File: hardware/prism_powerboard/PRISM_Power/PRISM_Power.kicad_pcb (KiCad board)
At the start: 2 copper layers, 48 parts, among them IC2 LP87564WRNFTQ1, J1 UJ32-21-C-H-G-HMT-LT-P24-TR, Q1 AO3400A, Q2 AO3400A, U1 STM32G031F6Px, U2 BQ25895RTW, U3 BQ297xy, U4 MAX17048G+T10

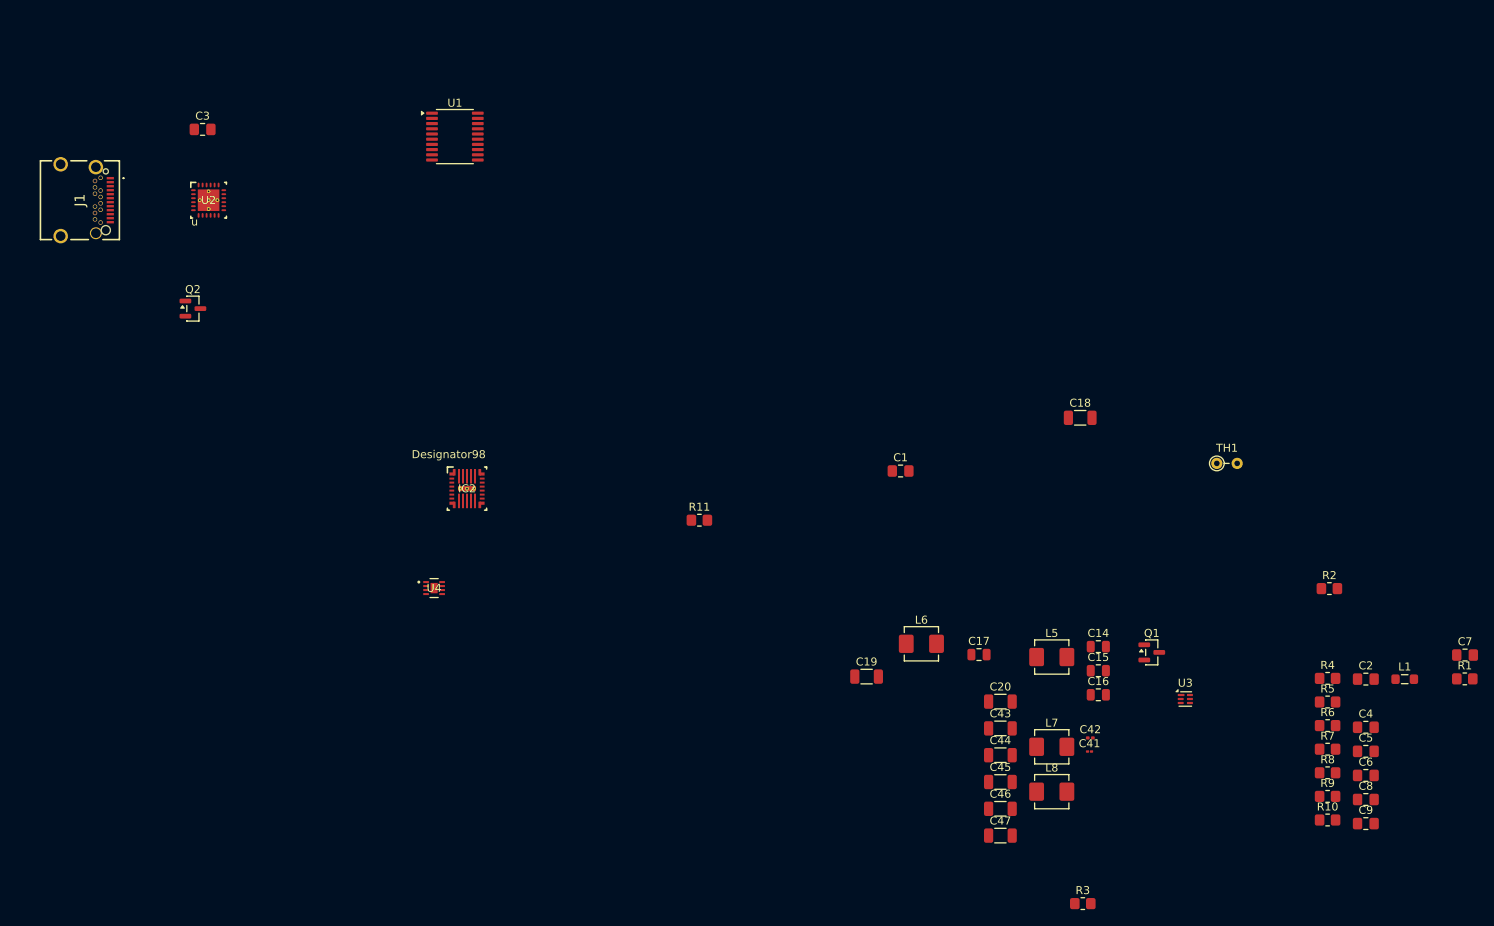
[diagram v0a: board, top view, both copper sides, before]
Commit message: PCB Routing
More PCB Routing and organizing components. Also fixed PMIC wrong Voltage labels/nets.
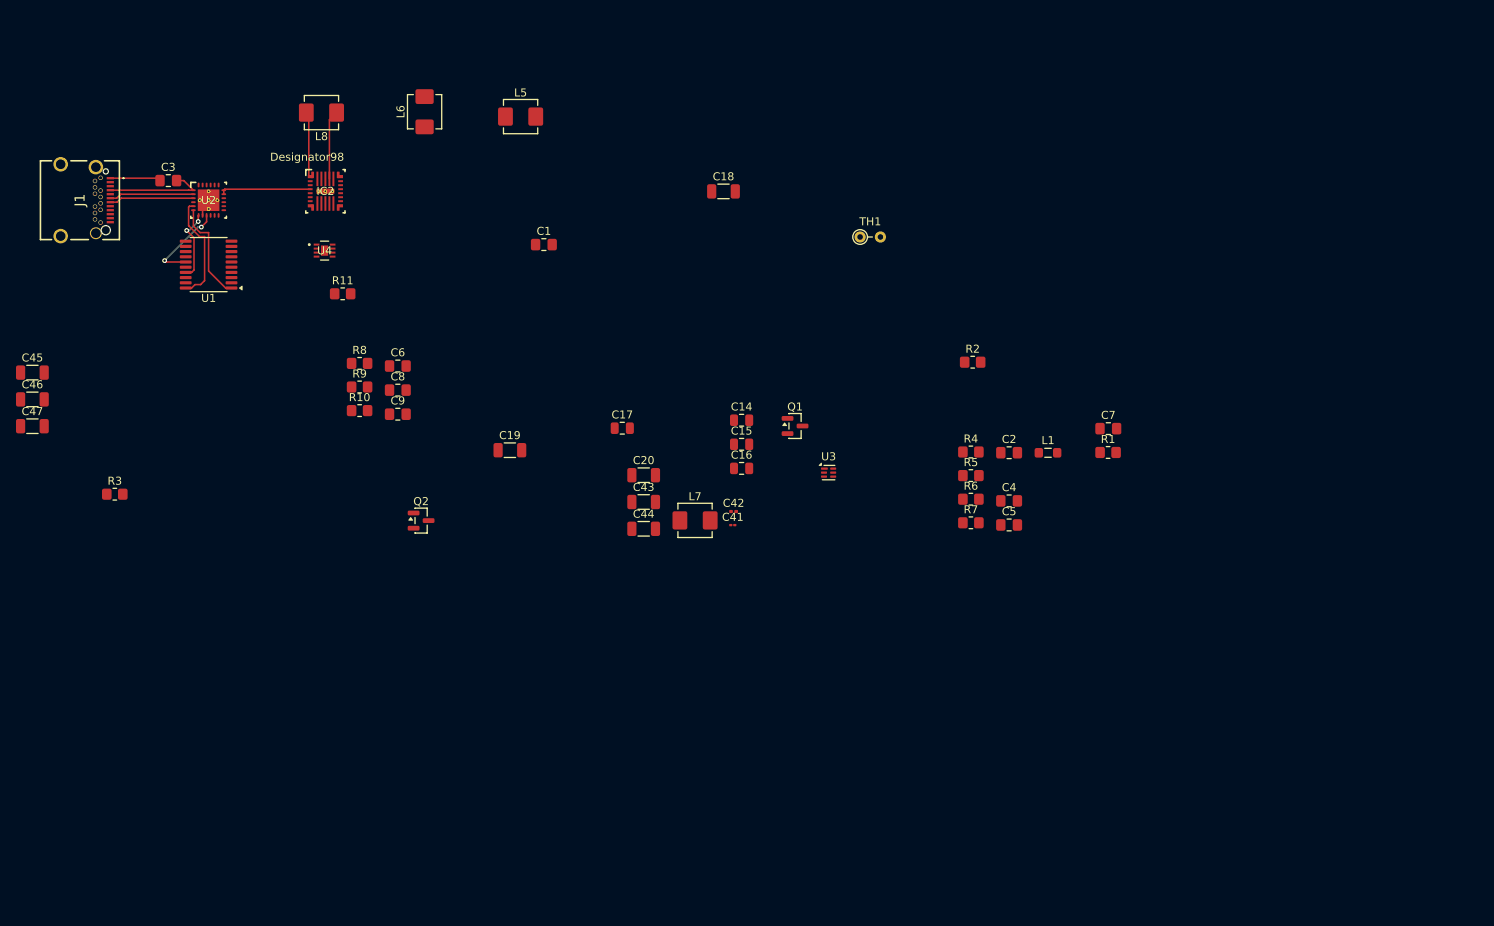
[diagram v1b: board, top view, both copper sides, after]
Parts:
- moved C45 131.4 mm to (76.5, 86.5)
- moved C46 131.4 mm to (76.5, 89.8)
- moved C47 131.4 mm to (76.5, 93.2)
- moved C6 131.4 mm to (122.2, 85.7)
- moved C8 131.4 mm to (122.2, 88.7)
- moved C9 131.4 mm to (122.2, 91.7)
- moved R10 131.4 mm to (117.4, 91.2)
- moved R3 131.4 mm to (86.8, 101.7)
- moved R8 131.4 mm to (117.4, 85.3)
- moved R9 131.4 mm to (117.4, 88.3)
- moved L8 124.7 mm to (112.6, 54.0), turned to 180 degrees
- moved L5 94.7 mm to (137.5, 54.5)
- moved L6 91.0 mm to (125.5, 53.9), turned to 90 degrees
- moved C16 52.8 mm to (165.1, 98.5)
- moved C4 52.8 mm to (198.6, 102.5)
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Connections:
- C18 pad 1: FB_B1 -> FB_B0
- C20 pad 1: FB_B1 -> FB_B0
- C44 pad 1: FB_B1 -> FB_B2
- C45 pad 1: FB_B1 -> FB_B2
- C46 pad 1: FB_B1 -> FB_B3
- C47 pad 1: FB_B1 -> FB_B3
- IC2 pad 1: FB_B1 -> FB_B2
- IC2 pad 21: FB_B1 -> FB_B3
- IC2 pad 5: SCL -> I2C_SCL_1V8
- IC2 pad 6: SDA -> I2C_SDA_1V8
- IC2 pad 8: FB_B1 -> FB_B0
- L5 pad 2: FB_B1 -> FB_B0
- L7 pad 2: FB_B1 -> FB_B2
- L8 pad 2: FB_B1 -> FB_B3
- R1 pad 2: FB_B1 -> +1V8
- R2 pad 1: FB_B1 -> +1V8
- R5 pad 2: FB_B1 -> +1V8
- R6 pad 2: FB_B1 -> +1V8
- U1 pad 4: FB_B1 -> +1V8_LDO
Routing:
- net GND: track 0.00 -> 19.4 mm
- net I2C_SCL_1V8: track 0.00 -> 13.8 mm
- net USB_VCC: track 0.00 -> 13.0 mm
- net I2C_SDA_1V8: track 0.00 -> 12.8 mm
- net CE_CHRG: track 0.00 -> 10.8 mm, vias 0 -> 2
- net USB_D_Plus: track 0.00 -> 10.6 mm
- net USB_D_Minus: track 0.00 -> 10.6 mm
- net INT_CHRG: track 0.00 -> 9.17 mm, vias 0 -> 2
- net SW_B3: track 0.00 -> 8.66 mm
- net FB_B1: track 0.00 -> 8.13 mm

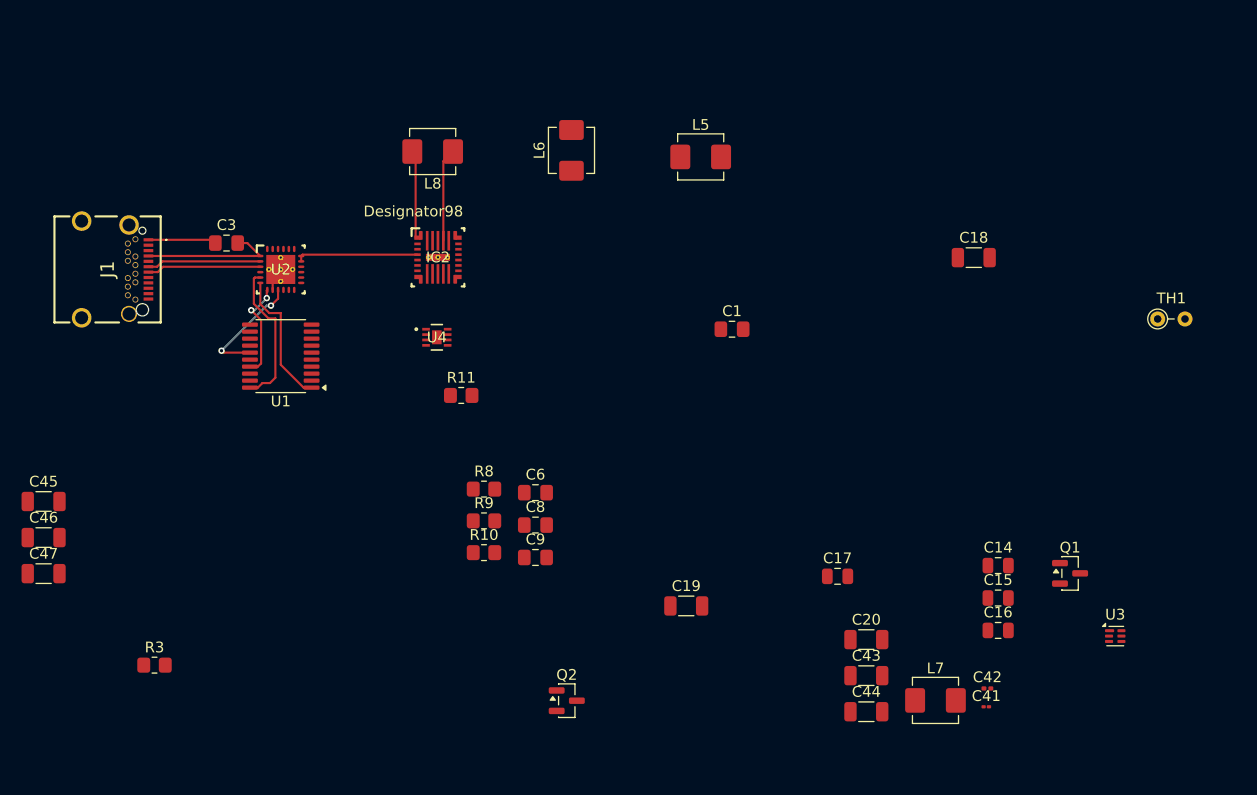
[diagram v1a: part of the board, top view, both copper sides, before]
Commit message: Circuit Board Layout Updates
More updates to the Layout, started organizing and added some simple routing, mostly for the power and feedback.
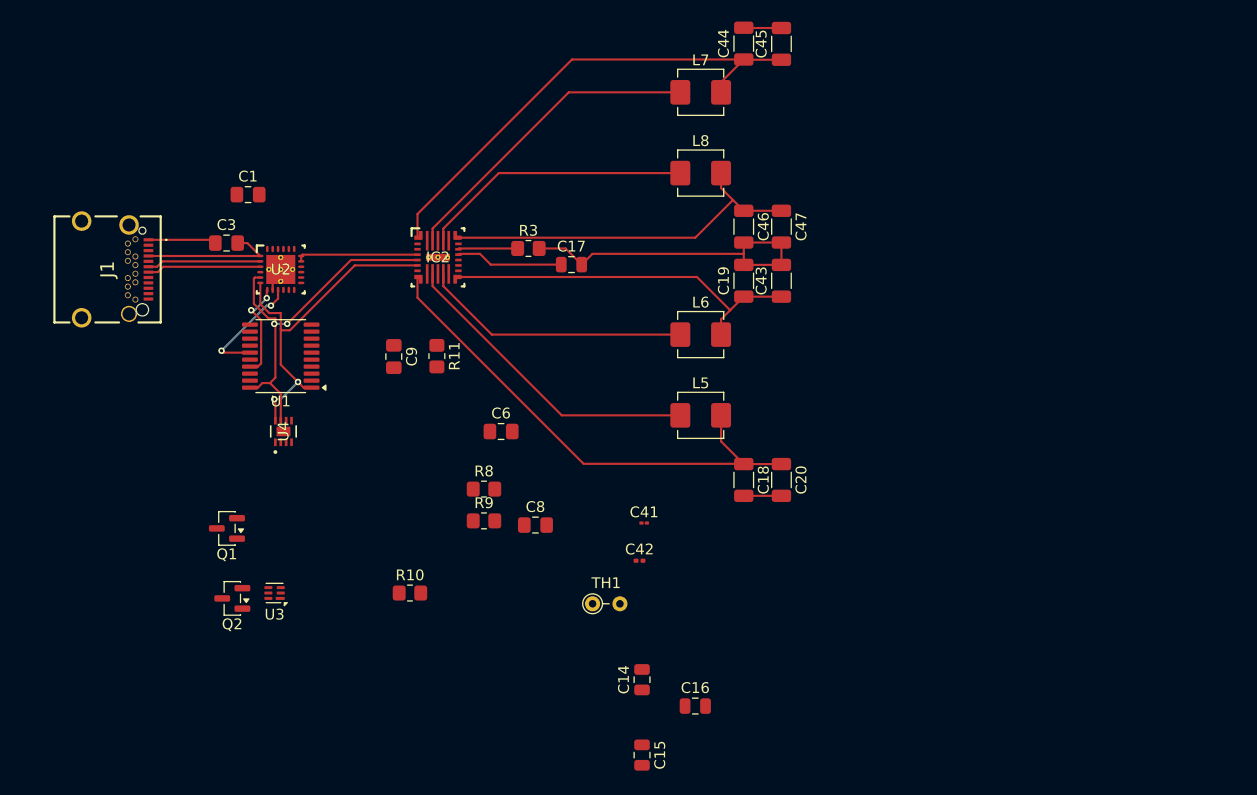
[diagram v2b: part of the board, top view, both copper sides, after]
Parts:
- moved C45 80.6 mm to (145.0, 44.0), turned to 90 degrees
- moved Q1 78.4 mm to (93.5, 89.0), turned to 180 degrees
- moved U3 78.2 mm to (97.9, 95.0), turned to 180 degrees
- moved C47 75.7 mm to (145.0, 61.0), turned to -90 degrees
- moved C46 71.1 mm to (141.5, 61.0), turned to -90 degrees
- moved C44 63.1 mm to (141.5, 44.0), turned to 90 degrees
- moved L7 60.5 mm to (137.5, 48.5)
- moved TH1 58.8 mm to (127.5, 96.0)
- moved R3 52.0 mm to (121.5, 63.0)
- moved C1 46.7 mm to (95.5, 58.0)
- moved C17 38.1 mm to (125.5, 64.5)
- moved C43 37.5 mm to (145.0, 66.0), turned to 90 degrees
- moved C15 36.1 mm to (132.1, 110.0), turned to -90 degrees
- moved C41 36.1 mm to (132.2, 88.5)
- moved C14 34.7 mm to (132.1, 103.0), turned to 90 degrees
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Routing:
- net FB_B0: track 0.00 -> 47.5 mm
- net FB_B2: track 0.00 -> 45.9 mm
- net GND: track 19.4 -> 57.5 mm
- net FB_B3: track 0.00 -> 34.8 mm
- net SW_B2: track 0.00 -> 29.4 mm
- net SW__B0: track 0.00 -> 29.1 mm
- net FB_B1: track 8.13 -> 34.4 mm
- net SW_B1: track 0.00 -> 25.0 mm
- net I2C_SDA_1V8: track 12.8 -> 32.9 mm, vias 0 -> 2
- net I2C_SCL_1V8: track 13.8 -> 33.4 mm, vias 0 -> 2
- net SW_B3: track 8.66 -> 25.3 mm
- net SYS_3V5: track 0.00 -> 10.00 mm
- net Net-(IC2-NINT): track 0.00 -> 5.53 mm

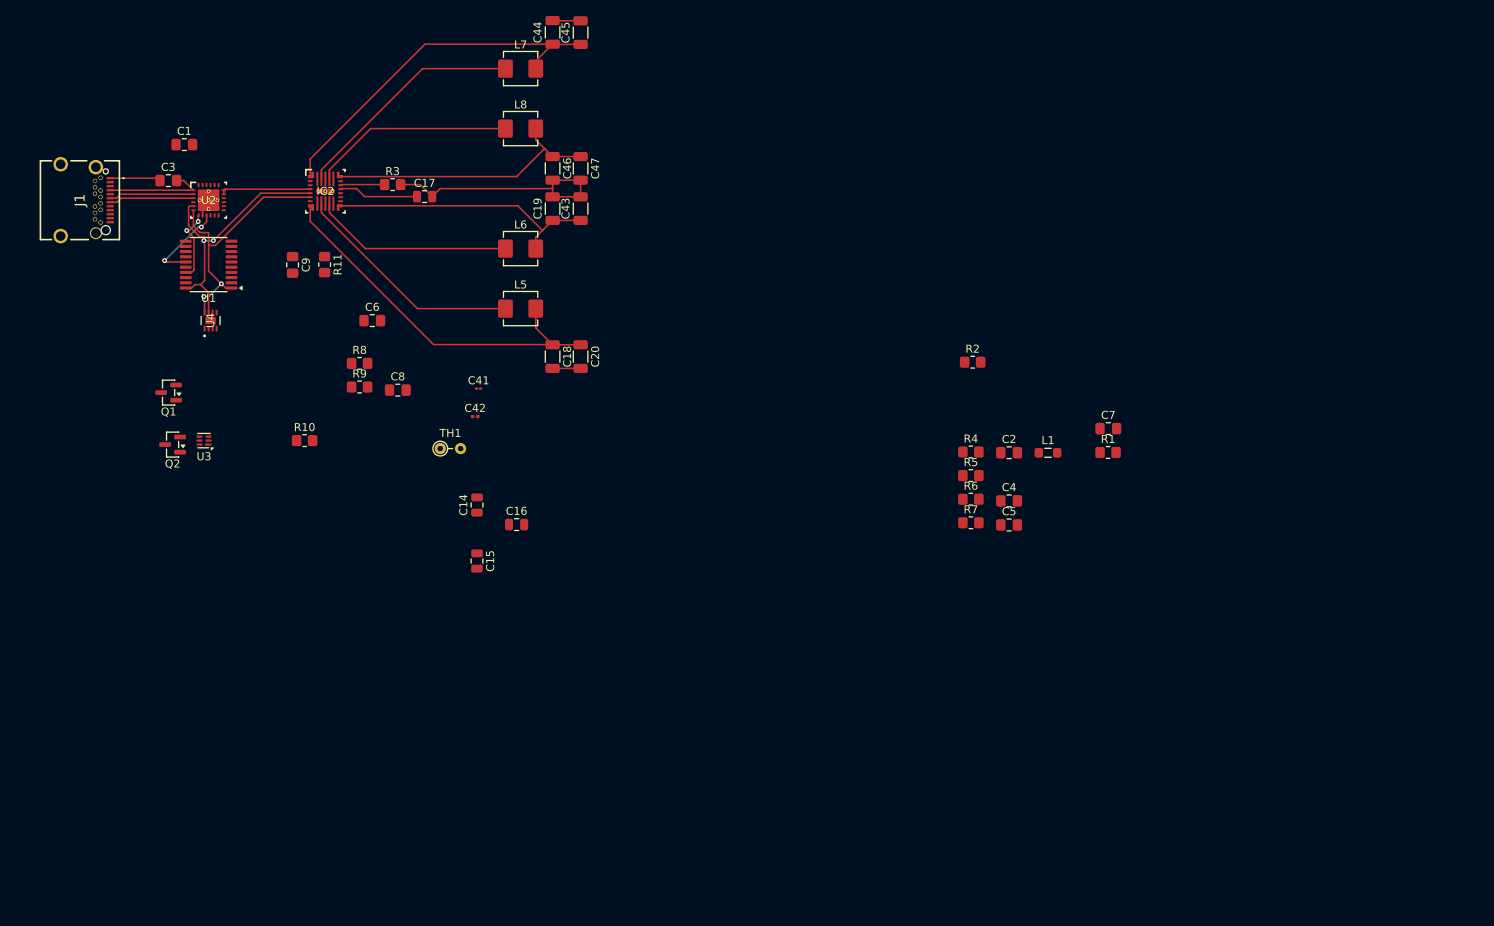
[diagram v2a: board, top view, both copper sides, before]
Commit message: Routing Updates
Nearly finished with Power Board PCB. Highly unoptimized and removed some pieces. Still need to ensure all needed connections are available.
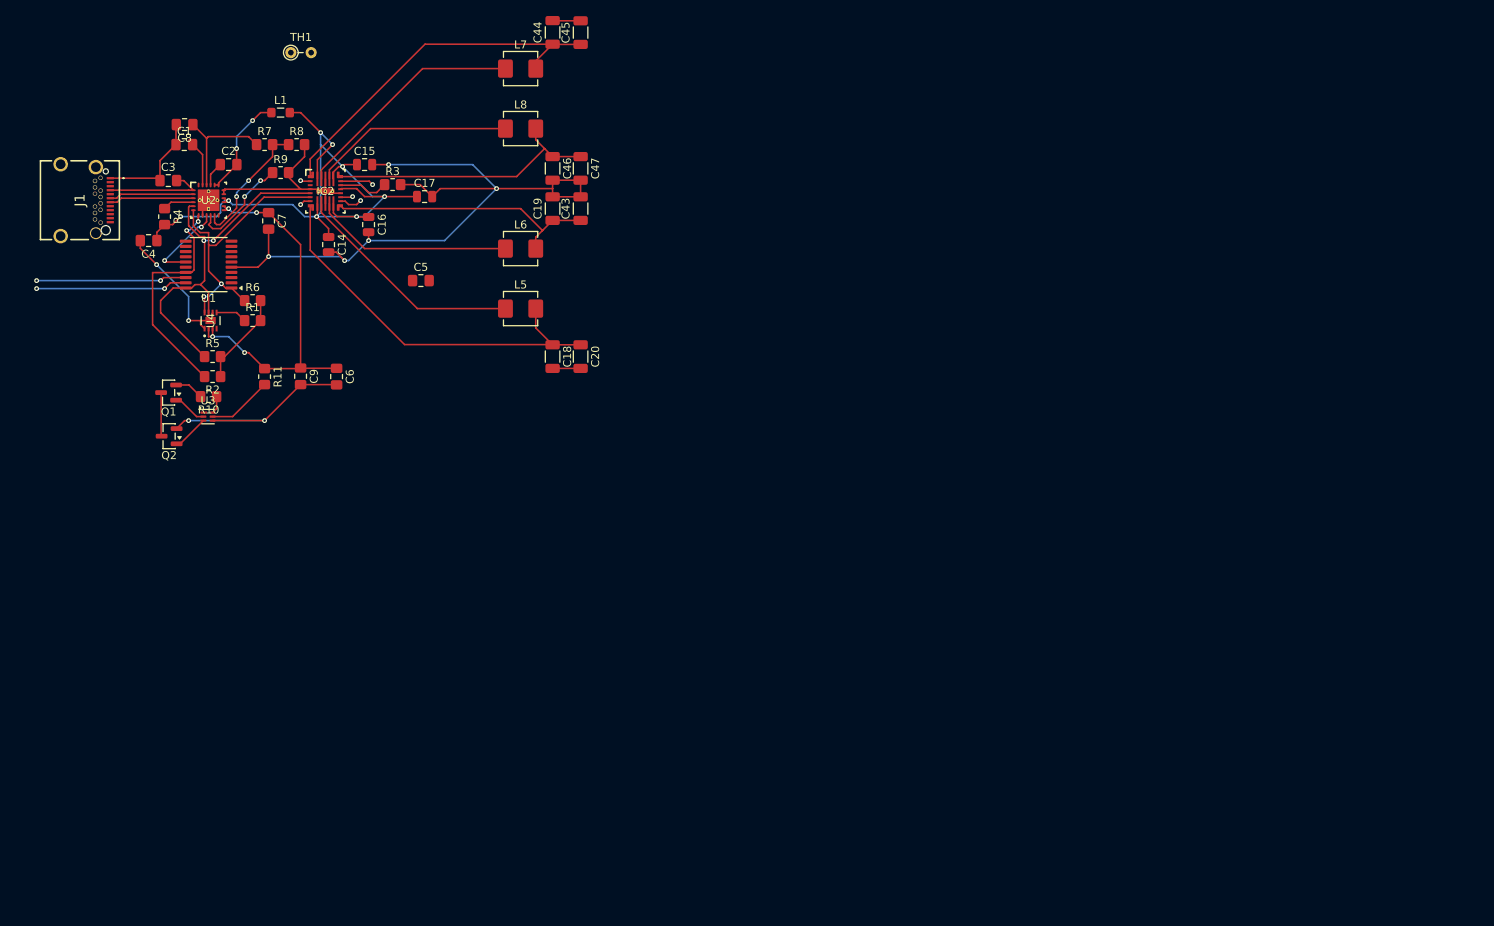
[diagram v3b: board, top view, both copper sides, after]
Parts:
- removed C41: 100nF, Capacitor_SMD:C_01005_0402Metric
- removed C42: 100nF, Capacitor_SMD:C_0201_0603Metric
- moved C4 112.4 mm to (91.0, 70.0), turned to 180 degrees
- moved R1 108.2 mm to (104.0, 80.0)
- moved C7 108.1 mm to (106.0, 67.5), turned to -90 degrees
- moved R4 105.0 mm to (93.0, 67.0), turned to -90 degrees
- moved L1 104.9 mm to (107.5, 54.0)
- moved C2 104.0 mm to (101.0, 60.5)
- moved R7 100.1 mm to (105.5, 58.0)
- moved R5 95.9 mm to (99.0, 84.5)
- moved R2 95.0 mm to (99.0, 87.0), turned to 180 degrees
- moved R6 93.2 mm to (104.0, 77.5)
- moved C5 79.6 mm to (125.0, 75.0)
- moved TH1 52.9 mm to (108.8, 46.5)
- moved C15 51.5 mm to (118.0, 60.5), turned to 0 degrees
- moved C8 42.6 mm to (95.5, 55.5), turned to 180 degrees
- moved C16 41.8 mm to (118.5, 68.0), turned to -90 degrees
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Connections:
- C4 pad 1: SYS -> SYS_3V5
- C5 pad 1: SYS -> SYS_3V5
- L1 pad 2: SYS -> SYS_3V5
- U2 pad 15: SYS -> SYS_3V5
- U2 pad 16: SYS -> SYS_3V5
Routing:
- net GND: track 57.5 -> 163.5 mm, vias 0 -> 7
- net SYS_3V5: track 10.00 -> 93.9 mm, vias 0 -> 8
- net +BATT: track 0.00 -> 47.4 mm, vias 0 -> 4
- net -BATT: track 0.00 -> 28.8 mm, vias 0 -> 2
- net INT_CHRG: track 9.17 -> 29.0 mm
- net SWCLK: track 0.00 -> 18.9 mm, vias 0 -> 2
- net SWDIO: track 0.00 -> 18.8 mm, vias 0 -> 2
- net Net-(U2-TS): track 0.00 -> 16.4 mm, vias 0 -> 2
- net Net-(U2-REGN): track 0.00 -> 15.0 mm
- net Net-(C2-Pad2): track 0.00 -> 13.1 mm, vias 0 -> 2
- net I2C_SCL_1V8: track 33.4 -> 46.5 mm
- net Net-(U2-ILIM): track 0.00 -> 12.9 mm, vias 0 -> 2
- net +1V8: track 0.00 -> 11.9 mm
- net Net-(U3-BAT): track 0.00 -> 8.16 mm
- net Net-(U2-PMID): track 0.00 -> 5.57 mm
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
